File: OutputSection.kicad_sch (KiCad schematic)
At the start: 1 part, among them U2 TUSB319-Q1

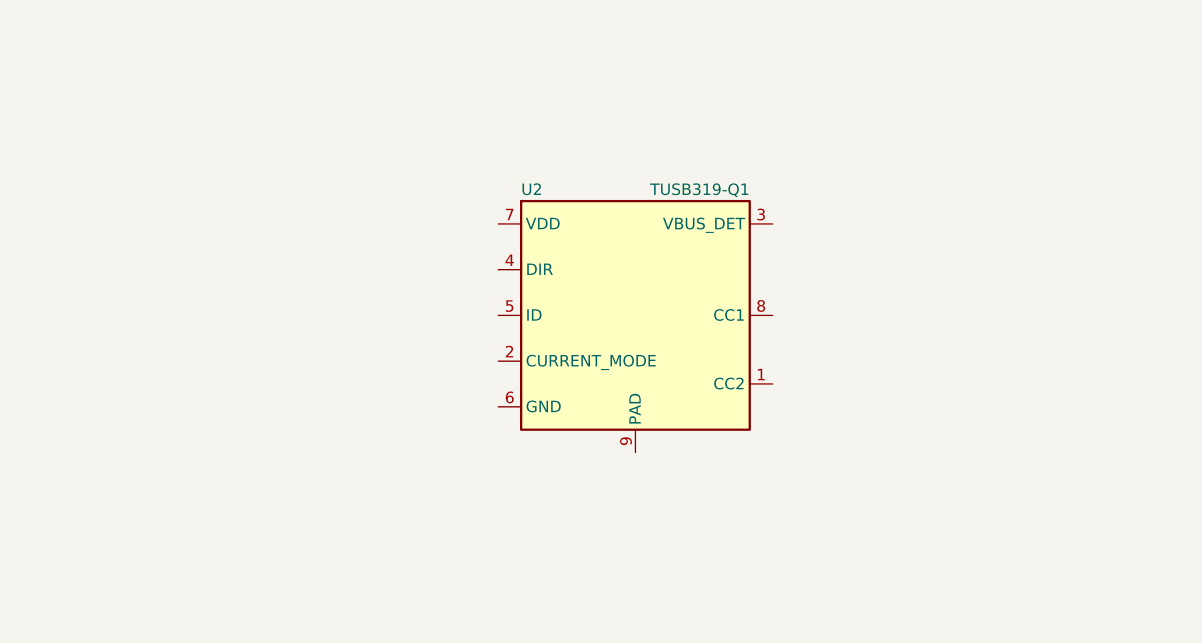
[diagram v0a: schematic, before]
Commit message: parts added to schematic
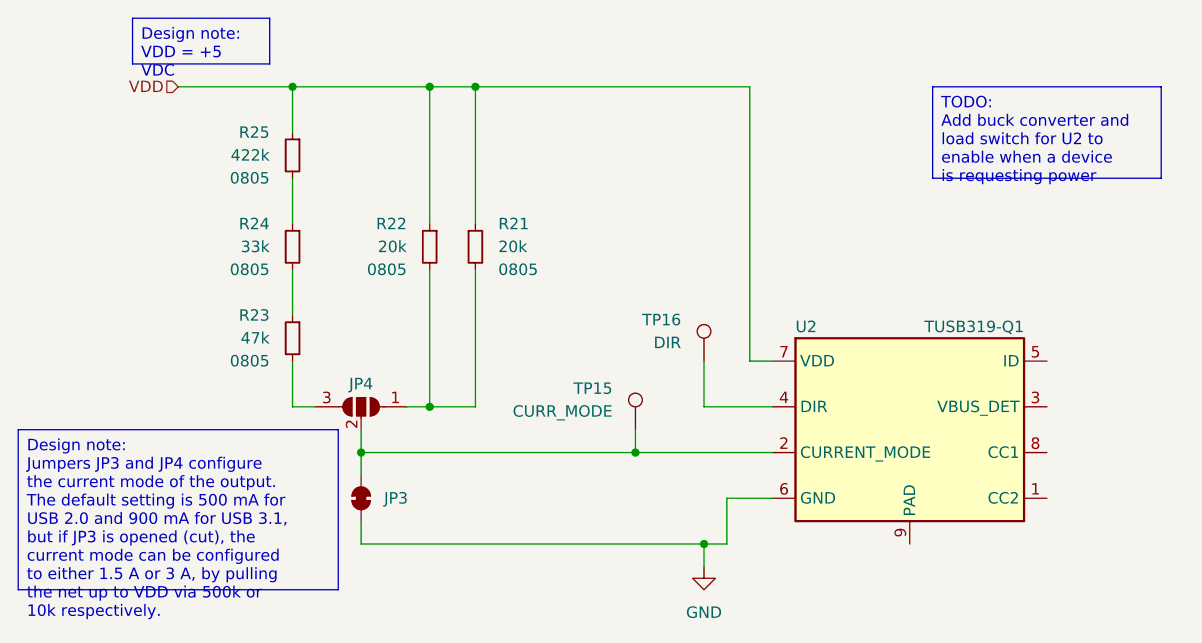
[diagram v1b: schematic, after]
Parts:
- added JP3: ~, Jumpers:JP-2_Bridged-RoundedPad1.0x1.5mm-Solder, symbol Jumpers:JP-2_Bridged-RoundedPad1.0x1.5mm-Solder
- added JP4: ~, Jumpers:JP-3_Open-RoundedPad1.0x1.5mm-Solder, symbol Jumpers:JP-3_Open-RoundedPad1.0x1.5mm-Solder
- added R21, R22: 20k, Resistors:R_0805_2012Metric, symbol Resistors:R0805-20k-0.5%-0.125W-SMD
- added R23: 47k, Resistors:R_0805_2012Metric, symbol Resistors:R0805-47k-1%-0.125W-SMD
- added R24: 33k, Resistors:R_0805_2012Metric, symbol Resistors:R0805-33k-0.5%-0.125W-SMD
- added R25: 422k, Resistors:R_0805_2012Metric, symbol Resistors:R0805-422k-1%-0.125W-SMD
- added TP15: CURR_MODE, Mech:TP-1.0mm-THM, symbol Mech:TP-1.0mm-THM
- added TP16: DIR, Mech:TP-1.0mm-THM, symbol Mech:TP-1.0mm-THM
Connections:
- net at U2.2 (CURRENT_MODE): now also JP3.2 (B), JP4.2 (C), TP15.1
- net at U2.4 (DIR): now also TP16.1
- net GND: now reaches U2.6 (GND)
- net GND: now also JP3.1 (A)
- net VDD: now reaches U2.7 (VDD)
- net VDD: now also R21.1, R22.1, R25.1
- new net: R24.1, R25.2
- new net: R23.1, R24.2
- new net: JP4.1 (A), R21.2, R22.2
- new net: JP4.3 (B), R23.2
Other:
- moved on the sheet: U2
